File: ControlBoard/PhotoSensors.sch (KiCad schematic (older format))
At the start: 58 parts, among them J12 Conn_01x01, J13 Conn_01x01, J14 Conn_01x01, J15 Conn_01x01, J16 Conn_01x06, J17 Conn_01x06, J18 Conn_01x06, U10 LMT85, U11 74HC138, U12 4051, U13 4051, U2 LM358

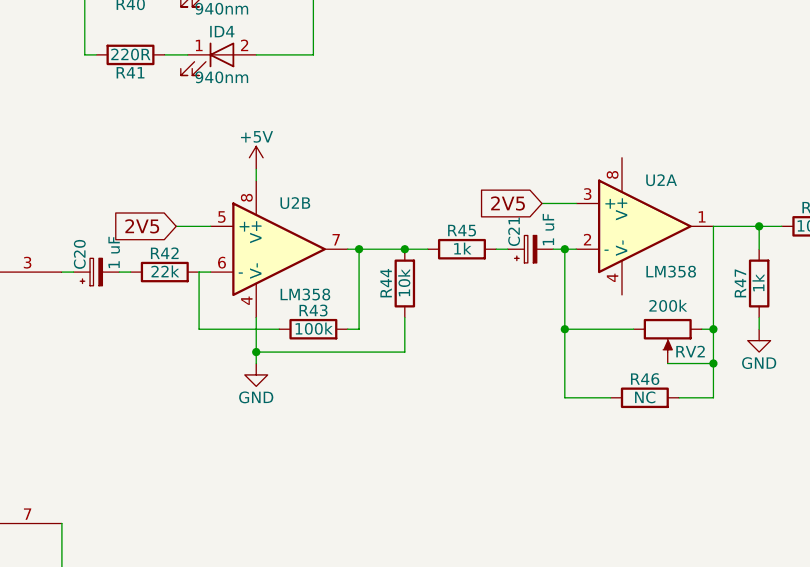
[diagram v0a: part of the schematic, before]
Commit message: Added CAD models
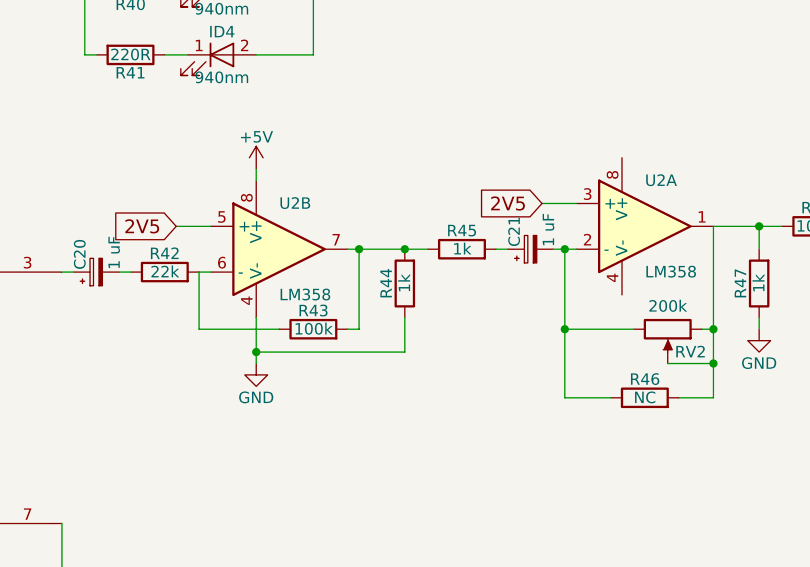
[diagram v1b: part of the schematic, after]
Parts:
- R44: value 10k -> 1k
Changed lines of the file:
@@
 $EndComp
 $Comp
-L +5V #PWR044
+L +5V #PWR046
 U 1 1 6147F8AB
 P 4850 2850
-F 0 "#PWR044" H 4850 2700 50  0001 C CNN
+F 0 "#PWR046" H 4850 2700 50  0001 C CNN
 F 1 "+5V" H 4850 2990 50  0000 C CNN
 F 2 "" H 4850 2850 50  0001 C CNN
@@
 $EndComp
 $Comp
-L GND #PWR045
+L GND #PWR047
 U 1 1 6147F8C9
 P 4850 4350
-F 0 "#PWR045" H 4850 4100 50  0001 C CNN
+F 0 "#PWR047" H 4850 4100 50  0001 C CNN
 F 1 "GND" H 4850 4200 50  0000 C CNN
 F 2 "" H 4850 4350 50  0001 C CNN
@@
 PHOTSELC
 $Comp
-L +5V #PWR046
+L +5V #PWR048
 U 1 1 6147FAC5
 P 4100 800
-F 0 "#PWR046" H 4100 650 50  0001 C CNN
+F 0 "#PWR048" H 4100 650 50  0001 C CNN
 F 1 "+5V" H 4100 940 50  0000 C CNN
 F 2 "" H 4100 800 50  0001 C CNN
@@
 $EndComp
 $Comp
-L GND #PWR047
+L GND #PWR049
 U 1 1 6147FAE8
 P 4100 2100
-F 0 "#PWR047" H 4100 1850 50  0001 C CNN
+F 0 "#PWR049" H 4100 1850 50  0001 C CNN
 F 1 "GND" H 4100 1950 50  0000 C CNN
 F 2 "" H 4100 2100 50  0001 C CNN
@@
 $EndComp
 $Comp
-L +5V #PWR048
+L +5V #PWR050
 U 1 1 6147FF6D
 P 6650 1100
-F 0 "#PWR048" H 6650 950 50  0001 C CNN
+F 0 "#PWR050" H 6650 950 50  0001 C CNN
 F 1 "+5V" H 6650 1240 50  0000 C CNN
 F 2 "" H 6650 1100 50  0001 C CNN
@@
 $EndComp
 $Comp
-L +5V #PWR049
+L +5V #PWR051
 U 1 1 614812EF
 P 1750 2400
-F 0 "#PWR049" H 1750 2250 50  0001 C CNN
+F 0 "#PWR051" H 1750 2250 50  0001 C CNN
 F 1 "+5V" H 1750 2540 50  0000 C CNN
 F 2 "" H 1750 2400 50  0001 C CNN
@@
 $EndComp
 $Comp
-L +5V #PWR050
+L +5V #PWR052
 U 1 1 61481486
 P 2050 700
-F 0 "#PWR050" H 2050 550 50  0001 C CNN
+F 0 "#PWR052" H 2050 550 50  0001 C CNN
 F 1 "+5V" H 2050 840 50  0000 C CNN
 F 2 "" H 2050 700 50  0001 C CNN
@@
 $EndComp
 $Comp
-L GND #PWR051
+L GND #PWR053
 U 1 1 614814CA
 P 2050 1150
-F 0 "#PWR051" H 2050 900 50  0001 C CNN
+F 0 "#PWR053" H 2050 900 50  0001 C CNN
 F 1 "GND" H 2050 1000 50  0000 C CNN
 F 2 "" H 2050 1150 50  0001 C CNN
@@
 $EndComp
 $Comp
-L GND #PWR052
+L GND #PWR054
 U 1 1 61481D45
 P 3800 4350
-F 0 "#PWR052" H 3800 4100 50  0001 C CNN
+F 0 "#PWR054" H 3800 4100 50  0001 C CNN
 F 1 "GND" H 3800 4200 50  0000 C CNN
 F 2 "" H 3800 4350 50  0001 C CNN
@@
 $EndComp
 $Comp
-L GND #PWR053
+L GND #PWR055
 U 1 1 61482BB1
 P 2200 4250
-F 0 "#PWR053" H 2200 4000 50  0001 C CNN
+F 0 "#PWR055" H 2200 4000 50  0001 C CNN
 F 1 "GND" H 2200 4100 50  0000 C CNN
 F 2 "" H 2200 4250 50  0001 C CNN
@@
 $EndComp
 $Comp
-L GND #PWR054
+L GND #PWR056
 U 1 1 61482FE8
 P 1850 4250
-F 0 "#PWR054" H 1850 4000 50  0001 C CNN
+F 0 "#PWR056" H 1850 4000 50  0001 C CNN
 F 1 "GND" H 1850 4100 50  0000 C CNN
 F 2 "" H 1850 4250 50  0001 C CNN
@@
 $EndComp
 $Comp
-L GND #PWR055
+L GND #PWR057
 U 1 1 614831F0
 P 1500 4250
-F 0 "#PWR055" H 1500 4000 50  0001 C CNN
+F 0 "#PWR057" H 1500 4000 50  0001 C CNN
 F 1 "GND" H 1500 4100 50  0000 C CNN
 F 2 "" H 1500 4250 50  0001 C CNN
@@
 $EndComp
 $Comp
-L GND #PWR056
+L GND #PWR058
 U 1 1 614834E7
 P 1150 4250
-F 0 "#PWR056" H 1150 4000 50  0001 C CNN
+F 0 "#PWR058" H 1150 4000 50  0001 C CNN
 F 1 "GND" H 1150 4100 50  0000 C CNN
 F 2 "" H 1150 4250 50  0001 C CNN
@@
 $EndComp
 $Comp
-L GND #PWR057
+L GND #PWR059
 U 1 1 614843BC
 P 6400 3350
-F 0 "#PWR057" H 6400 3100 50  0001 C CNN
+F 0 "#PWR059" H 6400 3100 50  0001 C CNN
 F 1 "GND" H 6400 3200 50  0000 C CNN
 F 2 "" H 6400 3350 50  0001 C CNN
@@
 $EndComp
 $Comp
-L +5V #PWR058
+L +5V #PWR060
 U 1 1 614844BC
 P 6400 2500
-F 0 "#PWR058" H 6400 2350 50  0001 C CNN
+F 0 "#PWR060" H 6400 2350 50  0001 C CNN
 F 1 "+5V" H 6400 2640 50  0000 C CNN
 F 2 "" H 6400 2500 50  0001 C CNN
@@
 $EndComp
 $Comp
-L GND #PWR059
+L GND #PWR061
 U 1 1 614885D2
 P 8600 3200
-F 0 "#PWR059" H 8600 2950 50  0001 C CNN
+F 0 "#PWR061" H 8600 2950 50  0001 C CNN
 F 1 "GND" H 8600 3050 50  0000 C CNN
 F 2 "" H 8600 3200 50  0001 C CNN
@@
 P 7050 3000
 F 0 "R44" V 7130 3000 50  0000 C CNN
-F 1 "10k" V 7050 3000 50  0000 C CNN
+F 1 "1k" V 7050 3000 50  0000 C CNN
 F 2 "Resistors_THT:R_Axial_DIN0207_L6.3mm_D2.5mm_P7.62mm_Horizontal" V 6980 3000 50  0001 C CNN
 F 3 "" H 7050 3000 50  0001 C CNN
@@
 $EndComp
 $Comp
-L GND #PWR060
+L GND #PWR062
 U 1 1 61489586
 P 9450 3200
-F 0 "#PWR060" H 9450 2950 50  0001 C CNN
+F 0 "#PWR062" H 9450 2950 50  0001 C CNN
 F 1 "GND" H 9450 3050 50  0000 C CNN
 F 2 "" H 9450 3200 50  0001 C CNN
@@
 $EndComp
 $Comp
-L GND #PWR061
+L GND #PWR063
 U 1 1 61489C2F
 P 9950 3200
-F 0 "#PWR061" H 9950 2950 50  0001 C CNN
+F 0 "#PWR063" H 9950 2950 50  0001 C CNN
 F 1 "GND" H 9950 3050 50  0000 C CNN
 F 2 "" H 9950 3200 50  0001 C CNN
@@
 $EndComp
 $Comp
-L GND #PWR062
+L GND #PWR064
 U 1 1 6148A4C2
 P 10250 3200
-F 0 "#PWR062" H 10250 2950 50  0001 C CNN
+F 0 "#PWR064" H 10250 2950 50  0001 C CNN
 F 1 "GND" H 10250 3050 50  0000 C CNN
 F 2 "" H 10250 3200 50  0001 C CNN
@@
 $EndComp
 $Comp
-L +5V #PWR063
+L +5V #PWR065
 U 1 1 614BCEBF
 P 5150 5850
-F 0 "#PWR063" H 5150 5700 50  0001 C CNN
+F 0 "#PWR065" H 5150 5700 50  0001 C CNN
 F 1 "+5V" H 5150 5990 50  0000 C CNN
 F 2 "" H 5150 5850 50  0001 C CNN
@@
 $EndComp
 $Comp
-L GND #PWR064
+L GND #PWR066
 U 1 1 614BCEC5
 P 5150 7350
-F 0 "#PWR064" H 5150 7100 50  0001 C CNN
+F 0 "#PWR066" H 5150 7100 50  0001 C CNN
 F 1 "GND" H 5150 7200 50  0000 C CNN
 F 2 "" H 5150 7350 50  0001 C CNN
@@
 $EndComp
 $Comp
-L GND #PWR065
+L GND #PWR067
 U 1 1 614BCF0A
 P 4100 7350
-F 0 "#PWR065" H 4100 7100 50  0001 C CNN
+F 0 "#PWR067" H 4100 7100 50  0001 C CNN
 F 1 "GND" H 4100 7200 50  0000 C CNN
 F 2 "" H 4100 7350 50  0001 C CNN
@@
 LIGHTLEVEL
 $Comp
-L +5V #PWR066
+L +5V #PWR068
 U 1 1 614C0527
 P 1950 4950
-F 0 "#PWR066" H 1950 4800 50  0001 C CNN
+F 0 "#PWR068" H 1950 4800 50  0001 C CNN
 F 1 "+5V" H 1950 5090 50  0000 C CNN
 F 2 "" H 1950 4950 50  0001 C CNN
@@
 $EndComp
 $Comp
-L GND #PWR067
+L GND #PWR069
 U 1 1 614C2B73
 P 3000 7100
-F 0 "#PWR067" H 3000 6850 50  0001 C CNN
+F 0 "#PWR069" H 3000 6850 50  0001 C CNN
 F 1 "GND" H 3000 6950 50  0000 C CNN
 F 2 "" H 3000 7100 50  0001 C CNN
@@
 $EndComp
 $Comp
-L GND #PWR068
+L GND #PWR070
 U 1 1 614C2DE0
 P 2650 7100
-F 0 "#PWR068" H 2650 6850 50  0001 C CNN
+F 0 "#PWR070" H 2650 6850 50  0001 C CNN
 F 1 "GND" H 2650 6950 50  0000 C CNN
 F 2 "" H 2650 7100 50  0001 C CNN
@@
 $EndComp
 $Comp
-L GND #PWR069
+L GND #PWR071
 U 1 1 614C2FCF
 P 2300 7100
-F 0 "#PWR069" H 2300 6850 50  0001 C CNN
+F 0 "#PWR071" H 2300 6850 50  0001 C CNN
 F 1 "GND" H 2300 6950 50  0000 C CNN
 F 2 "" H 2300 7100 50  0001 C CNN
@@
 $EndComp
 $Comp
-L GND #PWR070
+L GND #PWR072
 U 1 1 614C31BF
 P 1950 7100
-F 0 "#PWR070" H 1950 6850 50  0001 C CNN
+F 0 "#PWR072" H 1950 6850 50  0001 C CNN
 F 1 "GND" H 1950 6950 50  0000 C CNN
 F 2 "" H 1950 7100 50  0001 C CNN
@@
 $EndComp
 $Comp
-L GND #PWR071
+L GND #PWR073
 U 1 1 614CA69F
 P 1500 6700
-F 0 "#PWR071" H 1500 6450 50  0001 C CNN
+F 0 "#PWR073" H 1500 6450 50  0001 C CNN
 F 1 "GND" H 1500 6550 50  0000 C CNN
 F 2 "" H 1500 6700 50  0001 C CNN
@@
 $EndComp
 $Comp
-L +5V #PWR072
+L +5V #PWR074
 U 1 1 614CA9A1
 P 1500 5900
-F 0 "#PWR072" H 1500 5750 50  0001 C CNN
+F 0 "#PWR074" H 1500 5750 50  0001 C CNN
 F 1 "+5V" H 1500 6040 50  0000 C CNN
 F 2 "" H 1500 5900 50  0001 C CNN
@@
 $EndComp
 $Comp
-L +5V #PWR073
+L +5V #PWR075
 U 1 1 6148B87D
 P 4800 850
-F 0 "#PWR073" H 4800 700 50  0001 C CNN
+F 0 "#PWR075" H 4800 700 50  0001 C CNN
 F 1 "+5V" H 4800 990 50  0000 C CNN
 F 2 "" H 4800 850 50  0001 C CNN
@@
 $EndComp
 $Comp
-L GND #PWR074
+L GND #PWR076
 U 1 1 6148D946
 P 3450 4450
-F 0 "#PWR074" H 3450 4200 50  0001 C CNN
+F 0 "#PWR076" H 3450 4200 50  0001 C CNN
 F 1 "GND" H 3450 4300 50  0000 C CNN
 F 2 "" H 3450 4450 50  0001 C CNN
@@
 $EndComp
 $Comp
-L +5V #PWR075
+L +5V #PWR077
 U 1 1 6148DEB8
 P 2950 3850
-F 0 "#PWR075" H 2950 3700 50  0001 C CNN
+F 0 "#PWR077" H 2950 3700 50  0001 C CNN
 F 1 "+5V" H 2950 3990 50  0000 C CNN
 F 2 "" H 2950 3850 50  0001 C CNN
@@
 $EndComp
 $Comp
-L GND #PWR076
+L GND #PWR078
 U 1 1 61482B42
 P 5500 700
-F 0 "#PWR076" H 5500 450 50  0001 C CNN
+F 0 "#PWR078" H 5500 450 50  0001 C CNN
 F 1 "GND" H 5500 550 50  0000 C CNN
 F 2 "" H 5500 700 50  0001 C CNN
@@
 	3850 6250 3850 5400
 $Comp
-L GND #PWR077
+L GND #PWR079
 U 1 1 61484CD9
 P 3650 5800
-F 0 "#PWR077" H 3650 5550 50  0001 C CNN
+F 0 "#PWR079" H 3650 5550 50  0001 C CNN
 F 1 "GND" H 3650 5650 50  0000 C CNN
 F 2 "" H 3650 5800 50  0001 C CNN
@@
 	3650 5800 3650 5400
 $Comp
-L +5V #PWR078
+L +5V #PWR080
 U 1 1 61484F3C
 P 3400 5100
-F 0 "#PWR078" H 3400 4950 50  0001 C CNN
+F 0 "#PWR080" H 3400 4950 50  0001 C CNN
 F 1 "+5V" H 3400 5240 50  0000 C CNN
 F 2 "" H 3400 5100 50  0001 C CNN

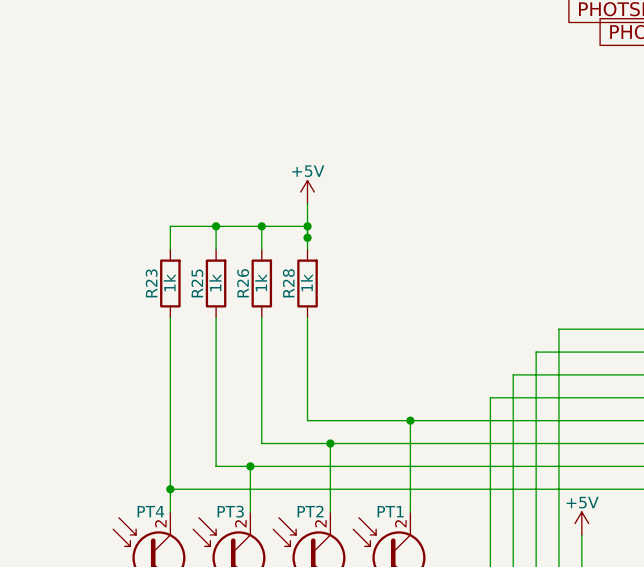
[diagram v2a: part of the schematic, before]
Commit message: Added second microphone to keypad
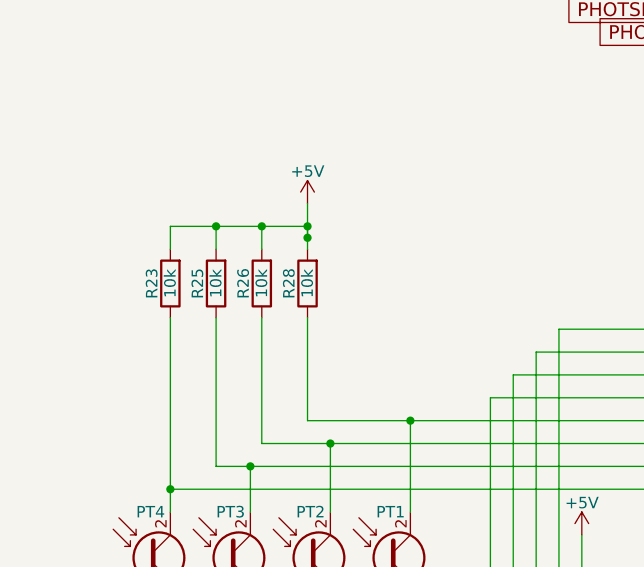
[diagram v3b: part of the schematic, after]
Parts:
- R23, R25, R26, R28: value 1k -> 10k
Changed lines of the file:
@@
 P 1750 2750
 F 0 "R28" V 1830 2750 50  0000 C CNN
-F 1 "1k" V 1750 2750 50  0000 C CNN
+F 1 "10k" V 1750 2750 50  0000 C CNN
 F 2 "Resistors_THT:R_Axial_DIN0207_L6.3mm_D2.5mm_P7.62mm_Horizontal" V 1680 2750 50  0001 C CNN
 F 3 "" H 1750 2750 50  0001 C CNN
@@
 P 1550 2750
 F 0 "R26" V 1630 2750 50  0000 C CNN
-F 1 "1k" V 1550 2750 50  0000 C CNN
+F 1 "10k" V 1550 2750 50  0000 C CNN
 F 2 "Resistors_THT:R_Axial_DIN0207_L6.3mm_D2.5mm_P7.62mm_Horizontal" V 1480 2750 50  0001 C CNN
 F 3 "" H 1550 2750 50  0001 C CNN
@@
 P 1350 2750
 F 0 "R25" V 1430 2750 50  0000 C CNN
-F 1 "1k" V 1350 2750 50  0000 C CNN
+F 1 "10k" V 1350 2750 50  0000 C CNN
 F 2 "Resistors_THT:R_Axial_DIN0207_L6.3mm_D2.5mm_P7.62mm_Horizontal" V 1280 2750 50  0001 C CNN
 F 3 "" H 1350 2750 50  0001 C CNN
@@
 P 1150 2750
 F 0 "R23" V 1230 2750 50  0000 C CNN
-F 1 "1k" V 1150 2750 50  0000 C CNN
+F 1 "10k" V 1150 2750 50  0000 C CNN
 F 2 "Resistors_THT:R_Axial_DIN0207_L6.3mm_D2.5mm_P7.62mm_Horizontal" V 1080 2750 50  0001 C CNN
 F 3 "" H 1150 2750 50  0001 C CNN

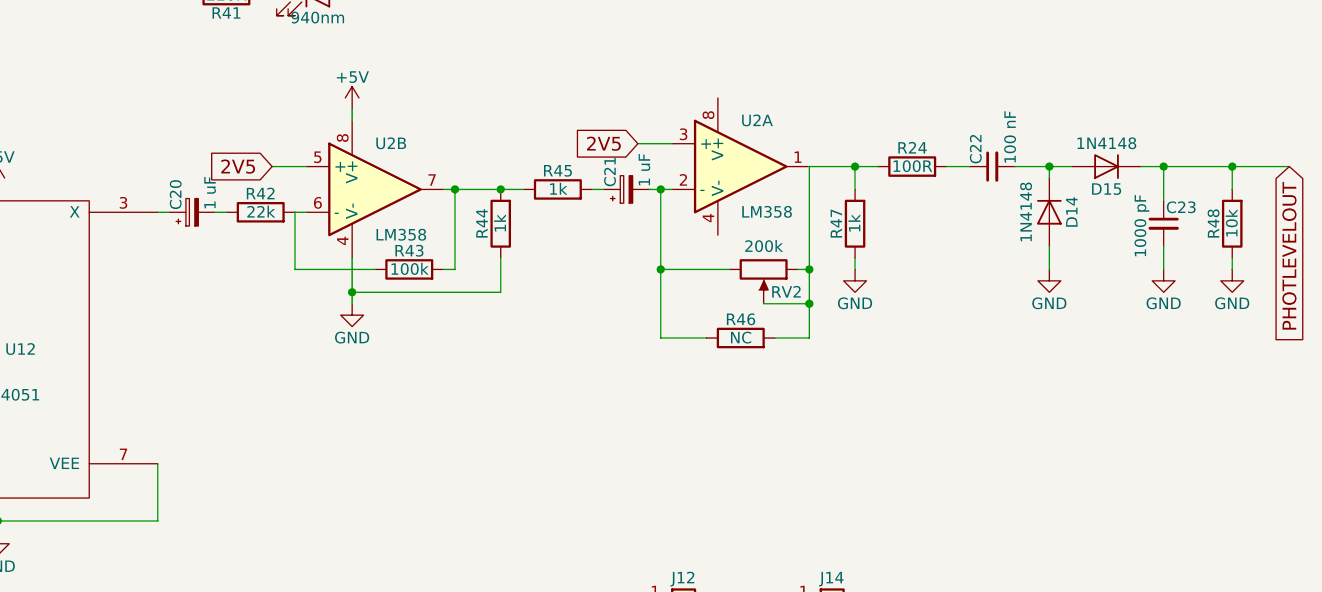
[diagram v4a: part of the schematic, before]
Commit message: Begin code for controlling robot with command line
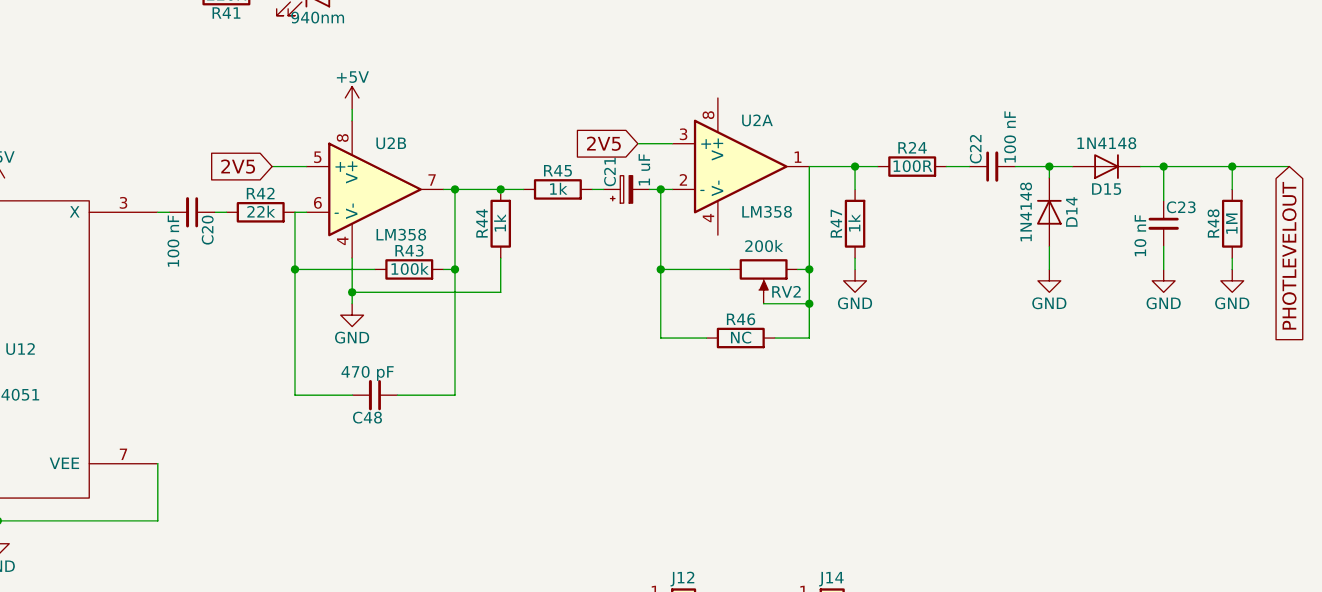
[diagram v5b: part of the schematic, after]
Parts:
- removed C20: 1 uF, Capacitors_THT:CP_Radial_D5.0mm_P2.50mm, symbol CP_Small
- added C20: 100 nF, Capacitors_THT:C_Disc_D5.0mm_W2.5mm_P5.00mm, symbol C_Small
- added C48: 470 pF, Capacitors_THT:C_Disc_D5.0mm_W2.5mm_P5.00mm, symbol C_Small
- C23: value 1000 pF -> 10 nF
- R48: value 10k -> 1M
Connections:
- net at U12.3 (X): now also C20.2
- net at R42.2, R43.1, U2.6 (-): now also C48.2
- net at R43.2, R44.2, R45.1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: now also C48.1
- net at R42.1: now also C20.1
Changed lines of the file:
@@
 P 9950 3000
 F 0 "C23" H 9960 3070 50  0000 L CNN
-F 1 "1000 pF" V 9850 2850 50  0000 L CNN
+F 1 "10 nF" V 9850 2850 50  0000 L CNN
 F 2 "Capacitors_THT:C_Disc_D5.0mm_W2.5mm_P5.00mm" H 9950 3000 50  0001 C CNN
 F 3 "" H 9950 3000 50  0001 C CNN
@@
 P 10250 3000
 F 0 "R48" V 10330 3000 50  0000 C CNN
-F 1 "10k" V 10250 3000 50  0000 C CNN
+F 1 "1M" V 10250 3000 50  0000 C CNN
 F 2 "Resistors_THT:R_Axial_DIN0207_L6.3mm_D2.5mm_P7.62mm_Horizontal" V 10180 3000 50  0001 C CNN
 F 3 "" H 10250 3000 50  0001 C CNN
@@
 2V5
 $Comp
-L CP_Small C20
-U 1 1 614AF73D
-P 5700 2950
-F 0 "C20" H 5710 3020 50  0000 L CNN
-F 1 "1 uF" H 5710 2870 50  0000 L CNN
-F 2 "Capacitors_THT:CP_Radial_D5.0mm_P2.50mm" H 5700 2950 50  0001 C CNN
-F 3 "" H 5700 2950 50  0001 C CNN
-	1    5700 2950
-	0    -1   -1   0
-$EndComp
-$Comp
 L R R42
 U 1 1 614AF930
@@
 Connection ~ 10250 2750
 Wire Wire Line
-	6850 3200 6850 2850
+	6850 2850 6850 3750
 Wire Wire Line
 	6800 2850 7150 2850
@@
 	6500 3200 6150 3200
 Wire Wire Line
-	6150 3200 6150 2950
+	6150 2950 6150 3750
 Wire Wire Line
 	6400 3300 7050 3300
@@
 Wire Wire Line
 	9100 2750 9000 2750
+$Comp
+L C_Small C20
+U 1 1 61721EF4
+P 5700 2950
+F 0 "C20" H 5710 3020 50  0000 L CNN
+F 1 "100 nF" H 5710 2870 50  0000 L CNN
+F 2 "Capacitors_THT:C_Disc_D5.0mm_W2.5mm_P5.00mm" H 5700 2950 50  0001 C CNN
+F 3 "" H 5700 2950 50  0001 C CNN
+	1    5700 2950
+	0    1    1    0
+$EndComp
+$Comp
+L C_Small C48
+U 1 1 6197E1B3
+P 6500 3750
+F 0 "C48" V 6600 3650 50  0000 L CNN
+F 1 "470 pF" V 6400 3600 50  0000 L CNN
+F 2 "Capacitors_THT:C_Disc_D5.0mm_W2.5mm_P5.00mm" H 6500 3750 50  0001 C CNN
+F 3 "" H 6500 3750 50  0001 C CNN
+	1    6500 3750
+	0    1    1    0
+$EndComp
+Wire Wire Line
+	6850 3750 6600 3750
+Connection ~ 6850 3200
+Wire Wire Line
+	6150 3750 6400 3750
+Connection ~ 6150 3200
 $EndSCHEMATC
